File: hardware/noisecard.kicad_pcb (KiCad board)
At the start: 2 copper layers, 85 x 50 mm, 32 parts, among them J1 Conn_ARM_SWD_TagConnect_TC203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, SW1 SW_DPDT_x2, U1 STM32G031F6Px, U2 LM3670MF

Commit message: schematic cleanup
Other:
- board text added: "NOTES 1. PRINTED CIRCUIT BOARD MADE FROM NEMA GRADE FR-4 EPOXY LAMINATE. 2. ALL DIMENSIONS ARE GIVEN IN MILLIMETERS. 3. CIRCUIT PATHS ARE FOR REFERENCE ONLY. 4. HOLE SIZES SHOWN ARE FINISHED DIAMETERS AFTER PLATING. 5. APPLY GREEN SOLDER MASK ON PLATED SURFACES. 6. SILKSCREEN TOP SIDE USING WHITE INK. 7. ALL VIAS ARE TENTED ON BOTH SIDES. 8. 2 COPPER LAYERS. 9. 0.8MM BOARD THICKNESS. 10. COPPER T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"
- board text removed: "NOTES 1. PRINTED CIRCUIT BOARD MADE FROM NEMA GRADE FR-4 EPOXY LAMINATE. 2. ALL DIMENSIONS ARE GIVEN IN MILLIMETERS. 3. CIRCUIT PATHS ARE FOR REFERENCE ONLY. 4. HOLE SIZES SHOWN ARE FINISHED DIAMETERS AFTER PLATING. 5. APPLY GREEN SOLDER MASK ON PLATED SURFACES. 6. SILKSCREEN TOP SIDE USING WHITE INK. 7. ALL VIAS ARE TENTED ON BOTH SIDES. 8. 2 COPPER LAYERS. 9. 1.6MM BOARD THICKNESS. 10. COPPER T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"
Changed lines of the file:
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@@
     (effects (font (size 2 2) (thickness 0.25) bold))
   )
-  (gr_text "NOTES\n\n 1. PRINTED CIRCUIT BOARD MADE FROM NEMA GRADE FR-4 EPOXY LAMINATE.\n 2. ALL DIMENSIONS ARE GIVEN IN MILLIMETERS.\n 3. CIRCUIT PATHS ARE FOR REFERENCE ONLY.\n 4. HOLE SIZES SHOWN ARE FINISHED DIAMETERS AFTER PLATING.\n 5. APPLY GREEN SOLDER MASK ON PLATED SURFACES.\n 6. SILKSCREEN TOP SIDE USING WHITE INK.\n 7. ALL VIAS ARE TENTED ON BOTH SIDES.\n 8. 2 COPPER LAYERS.\n 9. 1.6MM BOARD THICKNESS.\n10. COPPER THICKNESS 1 OZ." (at 38.75 139) (layer "Dwgs.User")
+  (gr_text "NOTES\n\n 1. PRINTED CIRCUIT BOARD MADE FROM NEMA GRADE FR-4 EPOXY LAMINATE.\n 2. ALL DIMENSIONS ARE GIVEN IN MILLIMETERS.\n 3. CIRCUIT PATHS ARE FOR REFERENCE ONLY.\n 4. HOLE SIZES SHOWN ARE FINISHED DIAMETERS AFTER PLATING.\n 5. APPLY GREEN SOLDER MASK ON PLATED SURFACES.\n 6. SILKSCREEN TOP SIDE USING WHITE INK.\n 7. ALL VIAS ARE TENTED ON BOTH SIDES.\n 8. 2 COPPER LAYERS.\n 9. 0.8MM BOARD THICKNESS.\n10. COPPER THICKNESS 1 OZ." (at 38.75 139) (layer "Dwgs.User")
     (effects (font (size 1.5 1.5) (thickness 0.1875)) (justify left top))
   )

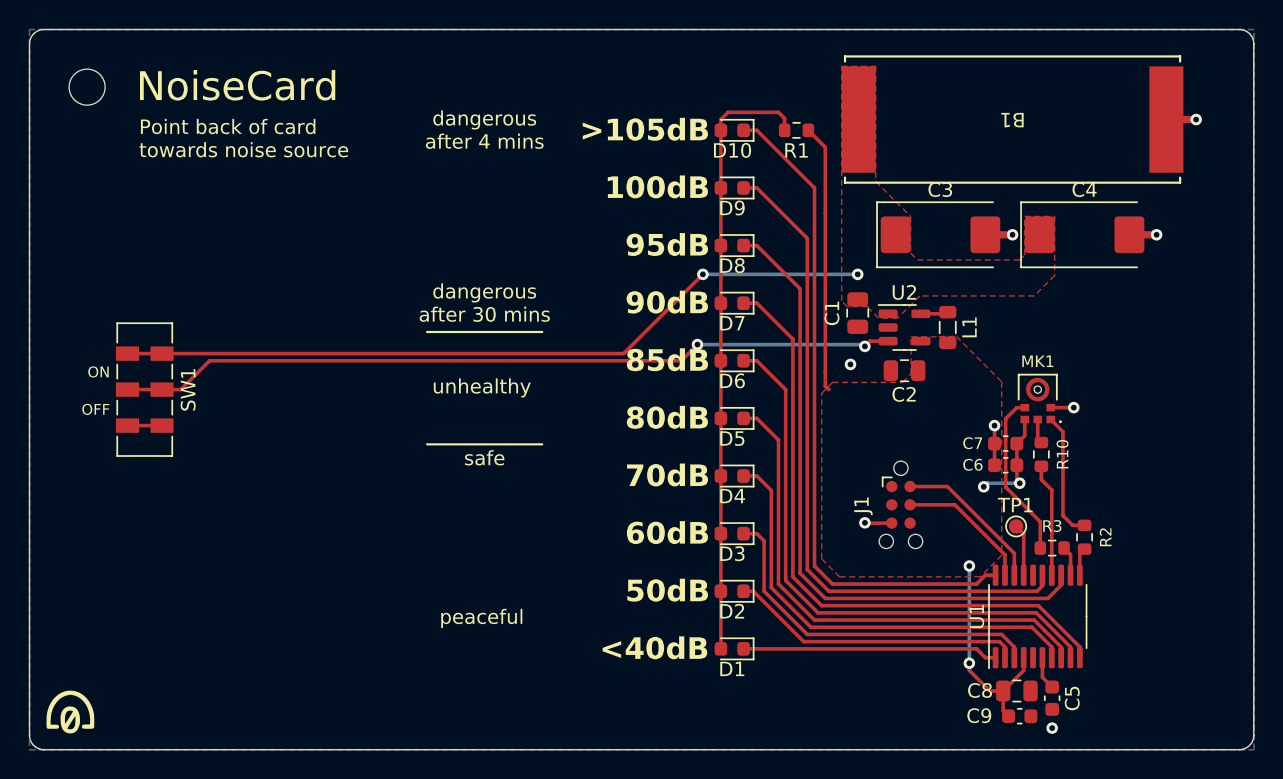
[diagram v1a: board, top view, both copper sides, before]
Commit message: add energy harvester and supercaps
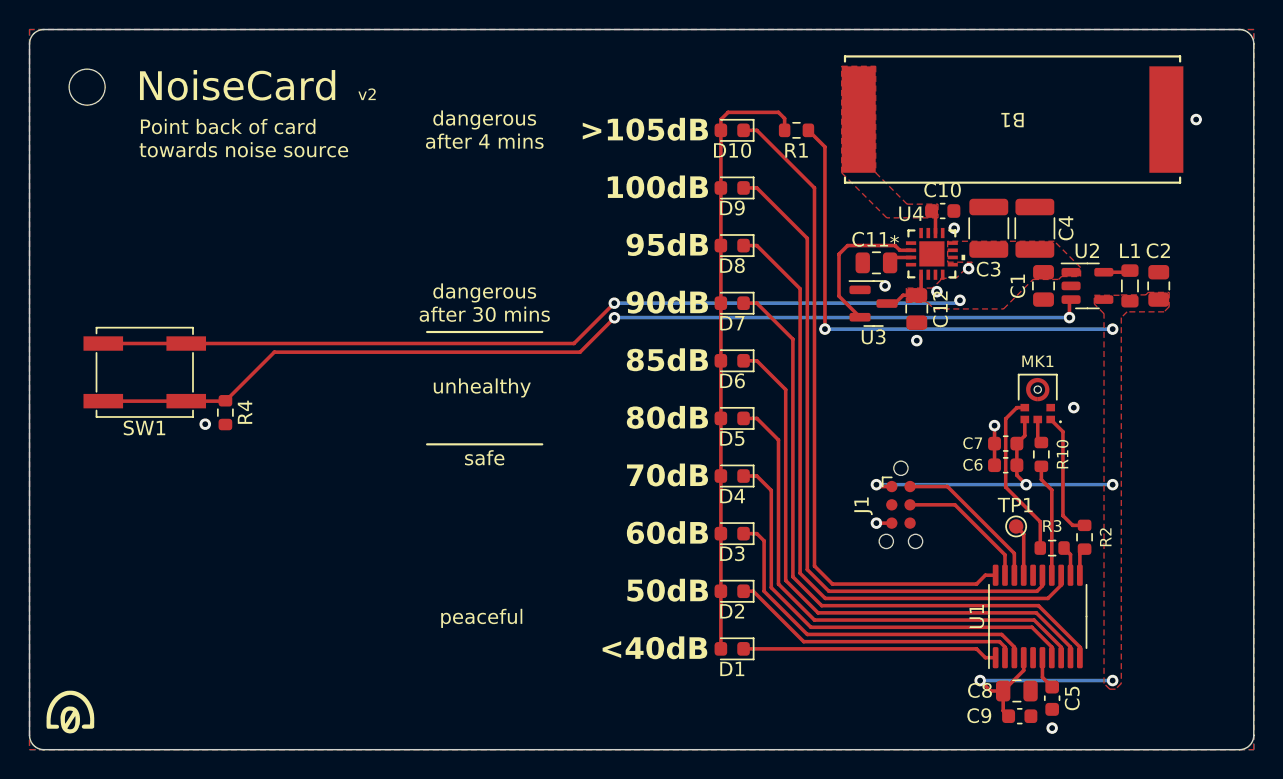
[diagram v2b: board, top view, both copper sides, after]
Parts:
- added C10: 5.6nF, Capacitor_SMD:C_0603_1608Metric, F.Cu at (173.4, 62.6)
- added C11: 2.2uF, Capacitor_SMD:C_0805_2012Metric, F.Cu at (168.8, 66.2)
- added C12: 2.2uF, Capacitor_SMD:C_0805_2012Metric, F.Cu at (171.6, 69.4)
- added R4: R_US, Resistor_SMD:R_0603_1608Metric, F.Cu at (123.6, 76.6)
- added U3: BD49KxxG, Package_TO_SOT_SMD:SOT-23, F.Cu at (168.6, 69.0)
- added U4: NEH2000BYJ, footprints:HWQFN16_SOT8076-1_NEX, F.Cu at (172.6, 65.6)
- B1: value KXOB25-02X8F-TR -> KXOB25-05X3F-TR
- C1: value 4u7 -> 4.7uF
- C2: value 10u -> 10uF
- C3, C4: value 330u -> 11mF; footprint Capacitor_Tantalum_SMD:CP_EIA-7343-15_Kemet-W -> Capacitor_SMD:C_1210_3225Metric
- C5, C6, C9: value 0.1U -> 0.1uF
- C7: value 200P -> 200pF
- C8: value 2U2 -> 2.2uF
- L1: value 10u -> 10uH
- SW1: value SW_DPDT_x2 -> SW_Push; footprint Button_Switch_SMD:SW_DPDT_CK_JS202011JCQN -> Button_Switch_SMD:SW_SPST_EVQP0
- moved C2 18.6 mm to (188.4, 67.8), turned to 90 degrees
- moved C1 13.0 mm to (180.4, 67.8)
- moved U2 13.0 mm to (183.4, 67.8)
- moved L1 13.0 mm to (186.4, 67.8)
- moved C4 3.48 mm to (179.8, 63.8), turned to 90 degrees
- moved C3 3.38 mm to (176.6, 63.8), turned to 90 degrees
- moved SW1 1.20 mm to (118.0, 73.8), turned to 180 degrees
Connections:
- B1 pad 2: VDC -> Net-(U4-VIN)
- C1 pad 1: VDC -> +BATT
- C3 pad 1: VDC -> +BATT
- C4 pad 1: VDC -> +BATT
- SW1 pad 1: VDC -> EN
- SW1 pad 2: EN -> +BATT
- U2 pad 1: VDC -> +BATT
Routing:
- net +BATT: track 0.00 -> 64.6 mm, vias 0 -> 2
- net VDC: track 53.0 -> 0.00 mm, vias 2 -> 0
- net +1V8: track 40.9 -> 72.7 mm, vias 4 -> 7
- net EN: track 54.3 -> 70.8 mm
- net GND: track 14.5 -> 3.82 mm, vias 8 -> 11
- net Net-(U3-VOUT): track 0.00 -> 10.4 mm
- net Net-(U4-VIN): track 0.00 -> 1.64 mm
- net Net-(U4-VREF): track 0.00 -> 1.61 mm
- added copper zone on F.Cu, net +BATT
- added copper zone on F.Cu, net Net-(U4-VIN)
- removed copper zone on F.Cu, net VDC
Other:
- board text added: "v2"
- board text removed: "OFF"
- board text removed: "ON"

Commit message: finish up rev2 design
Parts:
- removed H1: MountingHole_Pad, MountingHole:MountingHole_2.5mm
- removed J1: Conn_ARM_SWD_TagConnect_TC2030-NL, Connector:Tag-Connect_TC2030-IDC-NL_2x03_P1.27mm_Vertical
- removed TP1: TestPoint, TestPoint:TestPoint_Pad_D1.0mm
- added J2: Conn_02x07_Odd_Even, Connector_PinHeader_2.54mm:PinHeader_2x07_P2.54mm_Vertical, F.Cu at (171.3, 92.9)
- added TP2: TestPoint, TestPoint:TestPoint_THTPad_3.0x3.0mm_Drill1.5mm, F.Cu at (169.8, 57.6)
- added TP3: TestPoint, TestPoint:TestPoint_THTPad_3.0x3.0mm_Drill1.5mm, F.Cu at (191.1, 57.6)
- R4: value R_US -> 33k
- moved R1 5.15 mm to (158.8, 54.4)
- moved C2 4.26 mm to (187.7, 72.0), turned to 180 degrees
- moved R3 3.47 mm to (181.7, 82.6), turned to -90 degrees
- moved C8 2.71 mm to (178.3, 93.2)
- moved C5 2.71 mm to (180.8, 93.7)
- moved C9 2.71 mm to (178.6, 95.0)
- moved U1 2.71 mm to (179.8, 88.0)
- moved R2 2.65 mm to (183.2, 82.6)
- moved C12 2.61 mm to (173.8, 70.8)
- moved C3 2.58 mm to (178.8, 65.2)
- moved U2 2.58 mm to (185.7, 69.2)
- moved U3 2.58 mm to (170.8, 70.4)
- moved C1 2.58 mm to (182.6, 69.2)
- moved C4 2.58 mm to (182.0, 65.2)
- moved L1 2.58 mm to (188.6, 69.2)
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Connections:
- U1 pad 17: Net-(U1-PA12/PA10) -> unconnected-(U1-PA12/PA10-Pad17)
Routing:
- net +1V8: track 72.7 -> 91.9 mm, vias 7 -> 2
- net LED9: track 46.2 -> 40.2 mm
- net LED8: track 46.7 -> 41.5 mm
- net LED7: track 44.8 -> 39.8 mm
- net LED6: track 43.6 -> 39.0 mm
- net LED5: track 39.4 -> 35.1 mm
- net LED4: track 35.2 -> 31.2 mm
- net GND: track 3.82 -> 0.00 mm, vias 11 -> 13
- net Net-(D1-A): track 42.4 -> 38.6 mm
- net Net-(U1-PA12/PA10): track 3.60 -> 0.00 mm
- net LED3: track 31.0 -> 27.4 mm
- net MIC_DATA_OUT: track 7.86 -> 5.00 mm
- net MIC_WS: track 8.81 -> 6.11 mm
- net +BATT: track 64.6 -> 67.2 mm
- net MIC_BCLK: track 11.6 -> 9.09 mm, vias 0 -> 2
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- removed copper zone on F.Cu, net +1V8
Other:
- outline, holes or cut-outs redrawn
- board text added: "*"
- board text added: "1V8 B3-6 A6 A2 A0 C14/B9 GND"
- board text added: "SWDIO SWCLK B0-2/A8 A3 A1 C15 B7-8"
- board text added: "U1"
- board text added: "https://bitgloo.com"
- board text added: "pinout"
